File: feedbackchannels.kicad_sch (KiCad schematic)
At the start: 75 parts

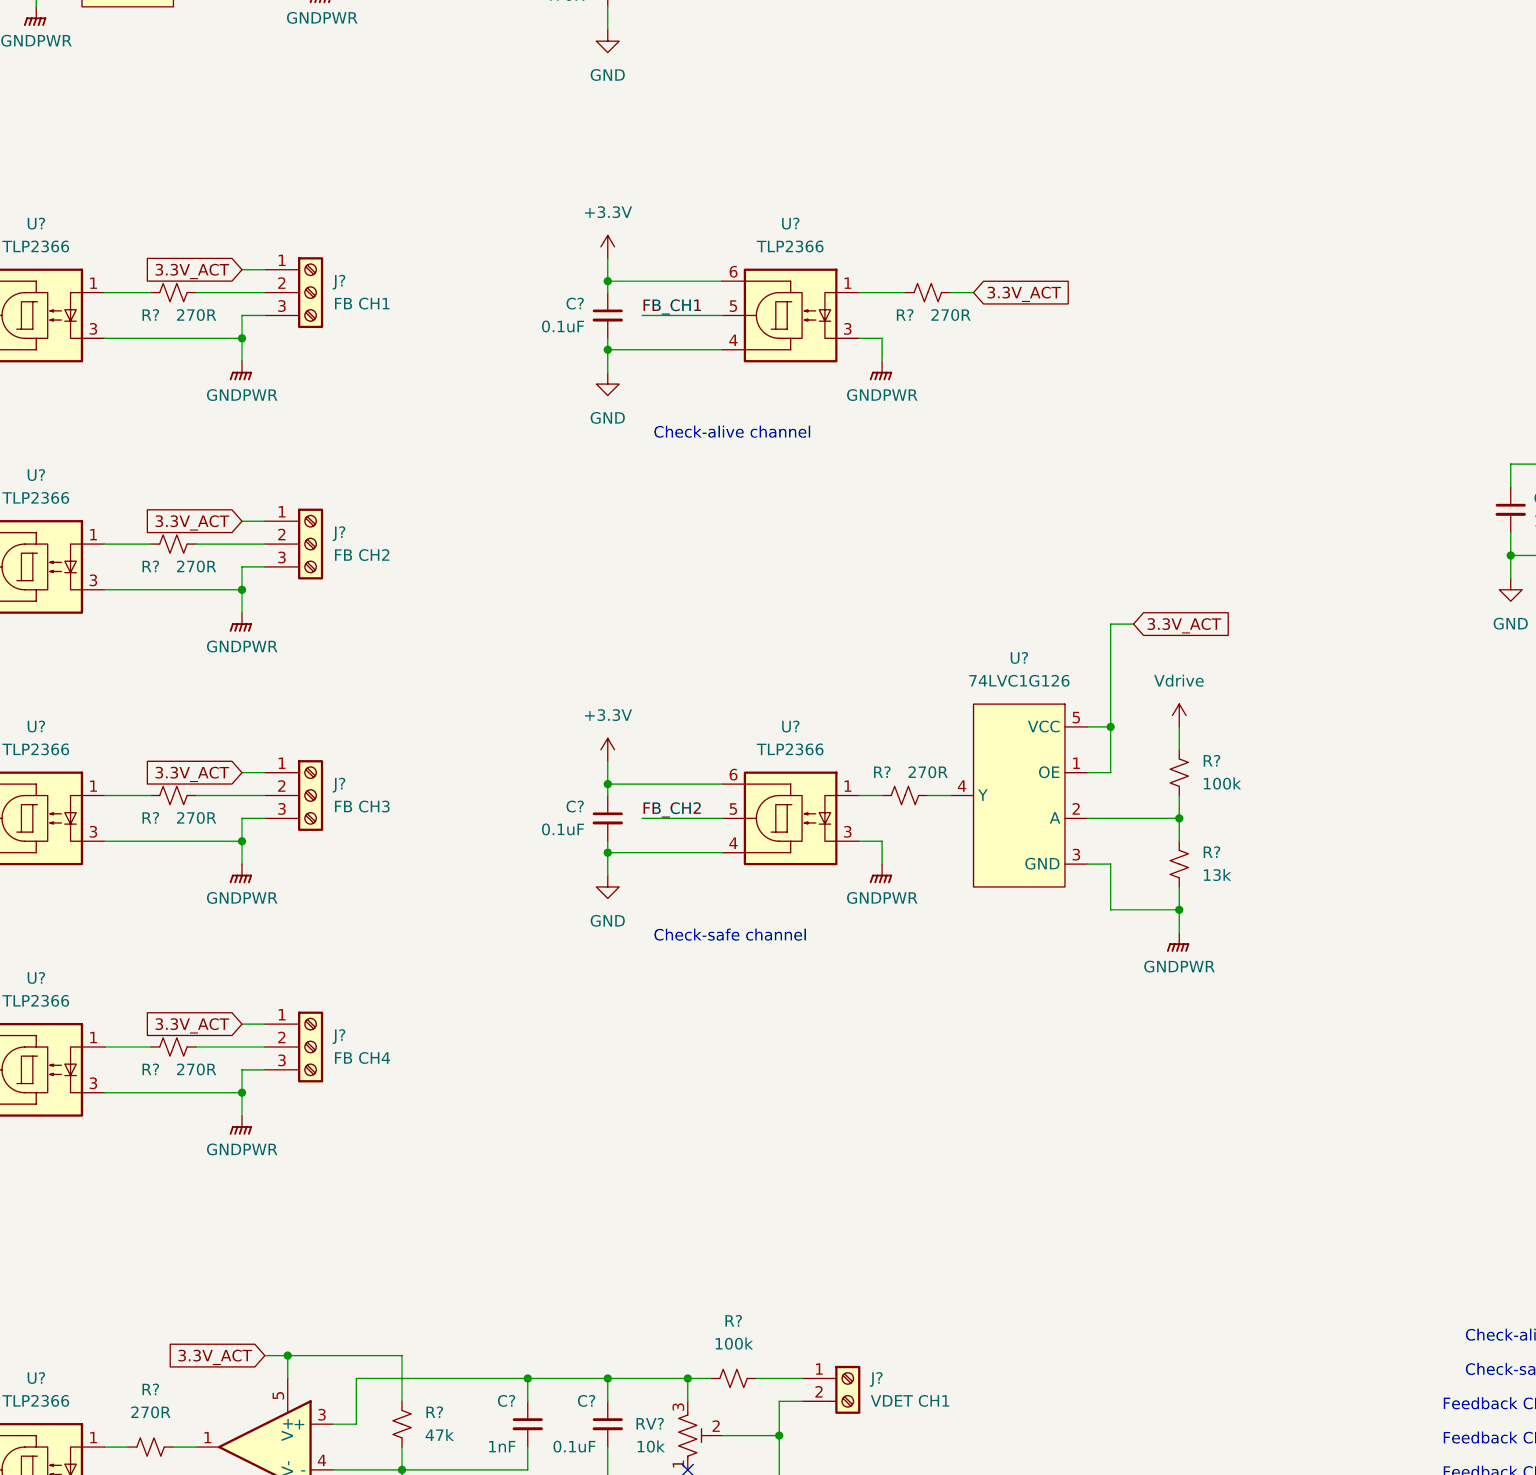
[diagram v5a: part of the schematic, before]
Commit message: add text
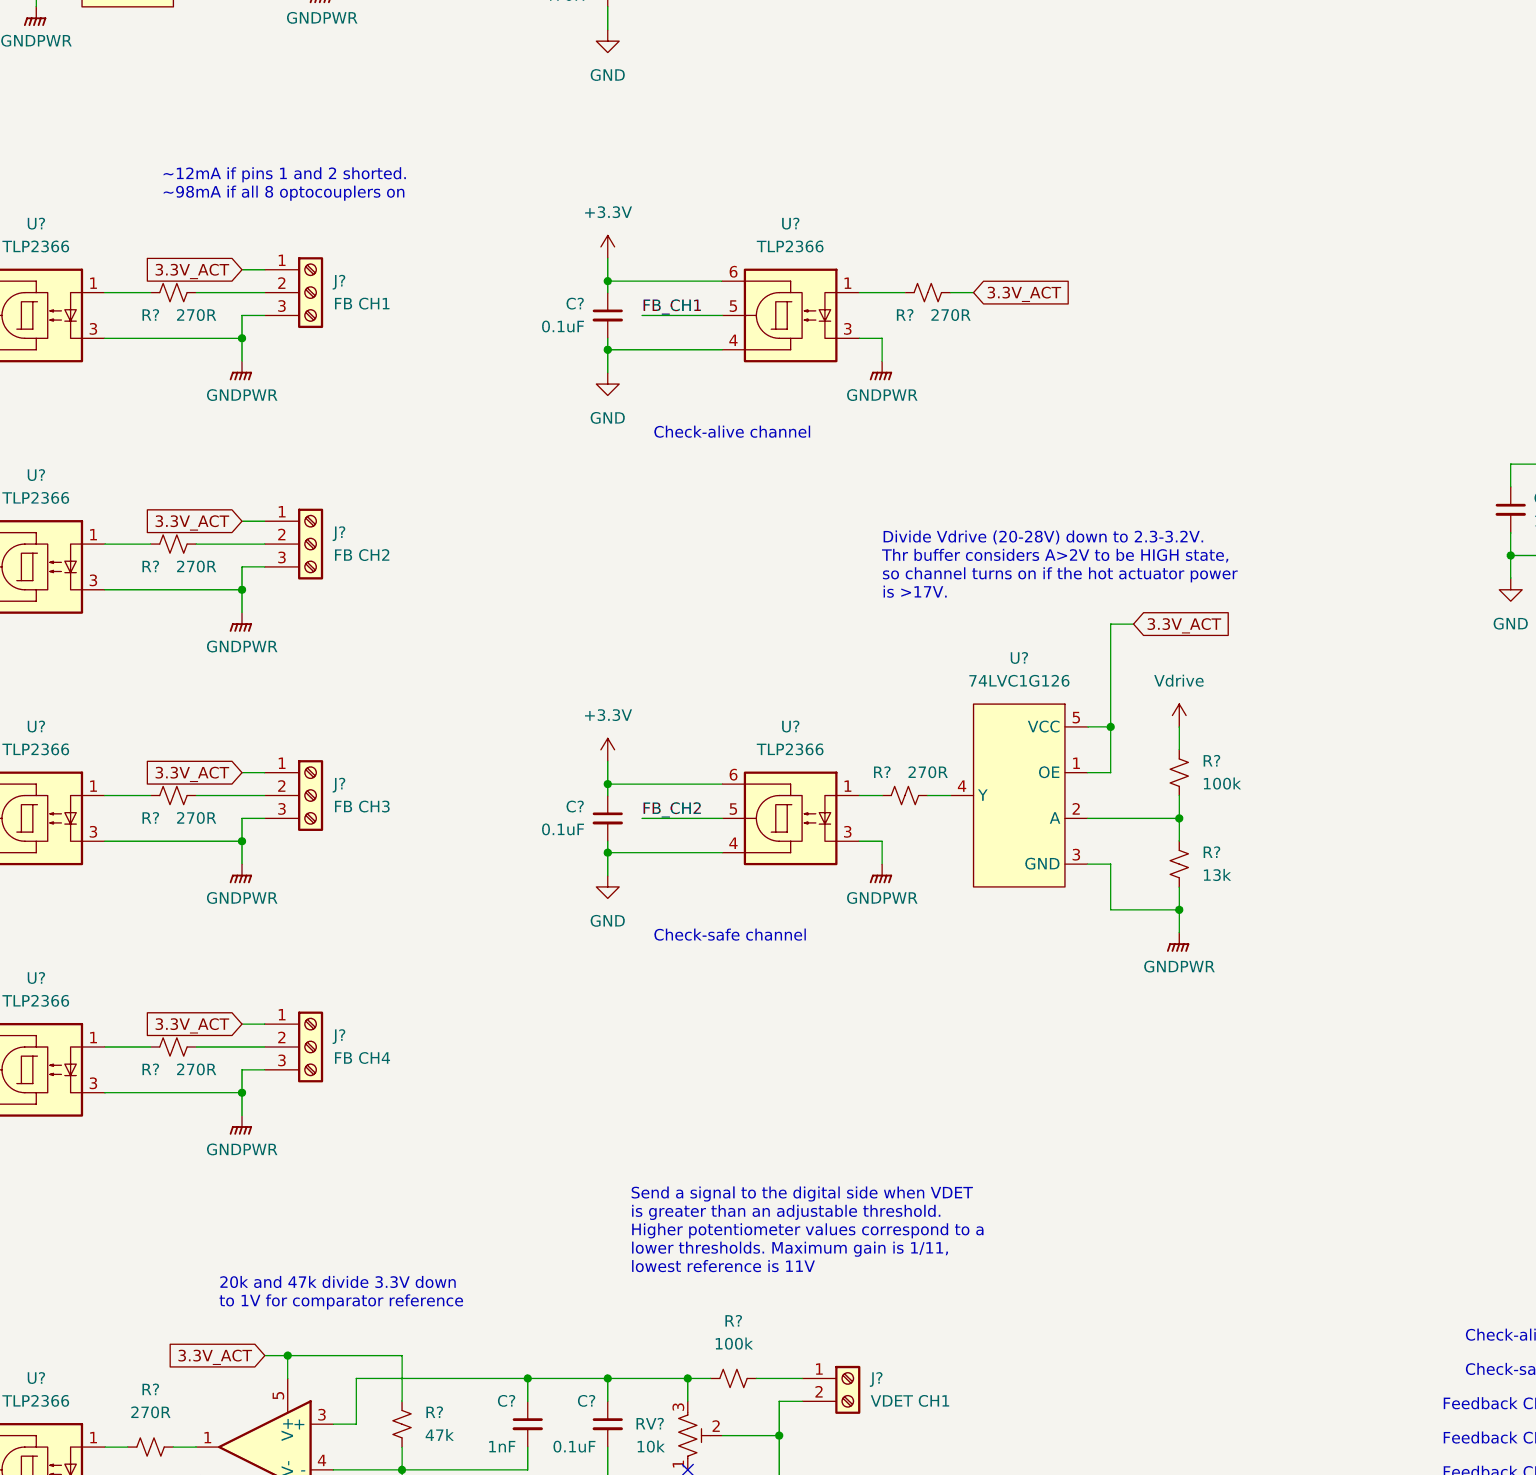
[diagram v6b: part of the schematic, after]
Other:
- note added: "20k and 47k divide 3.3V down to 1V for comparator reference"
- note added: "Divide Vdrive (20-28V) down to 2.3-3.2V. Thr buffer considers A>2V to be HIGH state, so channel turns on if the hot actuator power is >17V."
- note added: "Send a signal to the digital side when VDET is greater than an adjustable threshold. Higher potentiometer values correspond to a lower thresholds. Maximum gain is 1/11, lowest reference is 11V"
- note added: "~12mA if pins 1 and 2 shorted. ~98mA if all 8 optocouplers on"

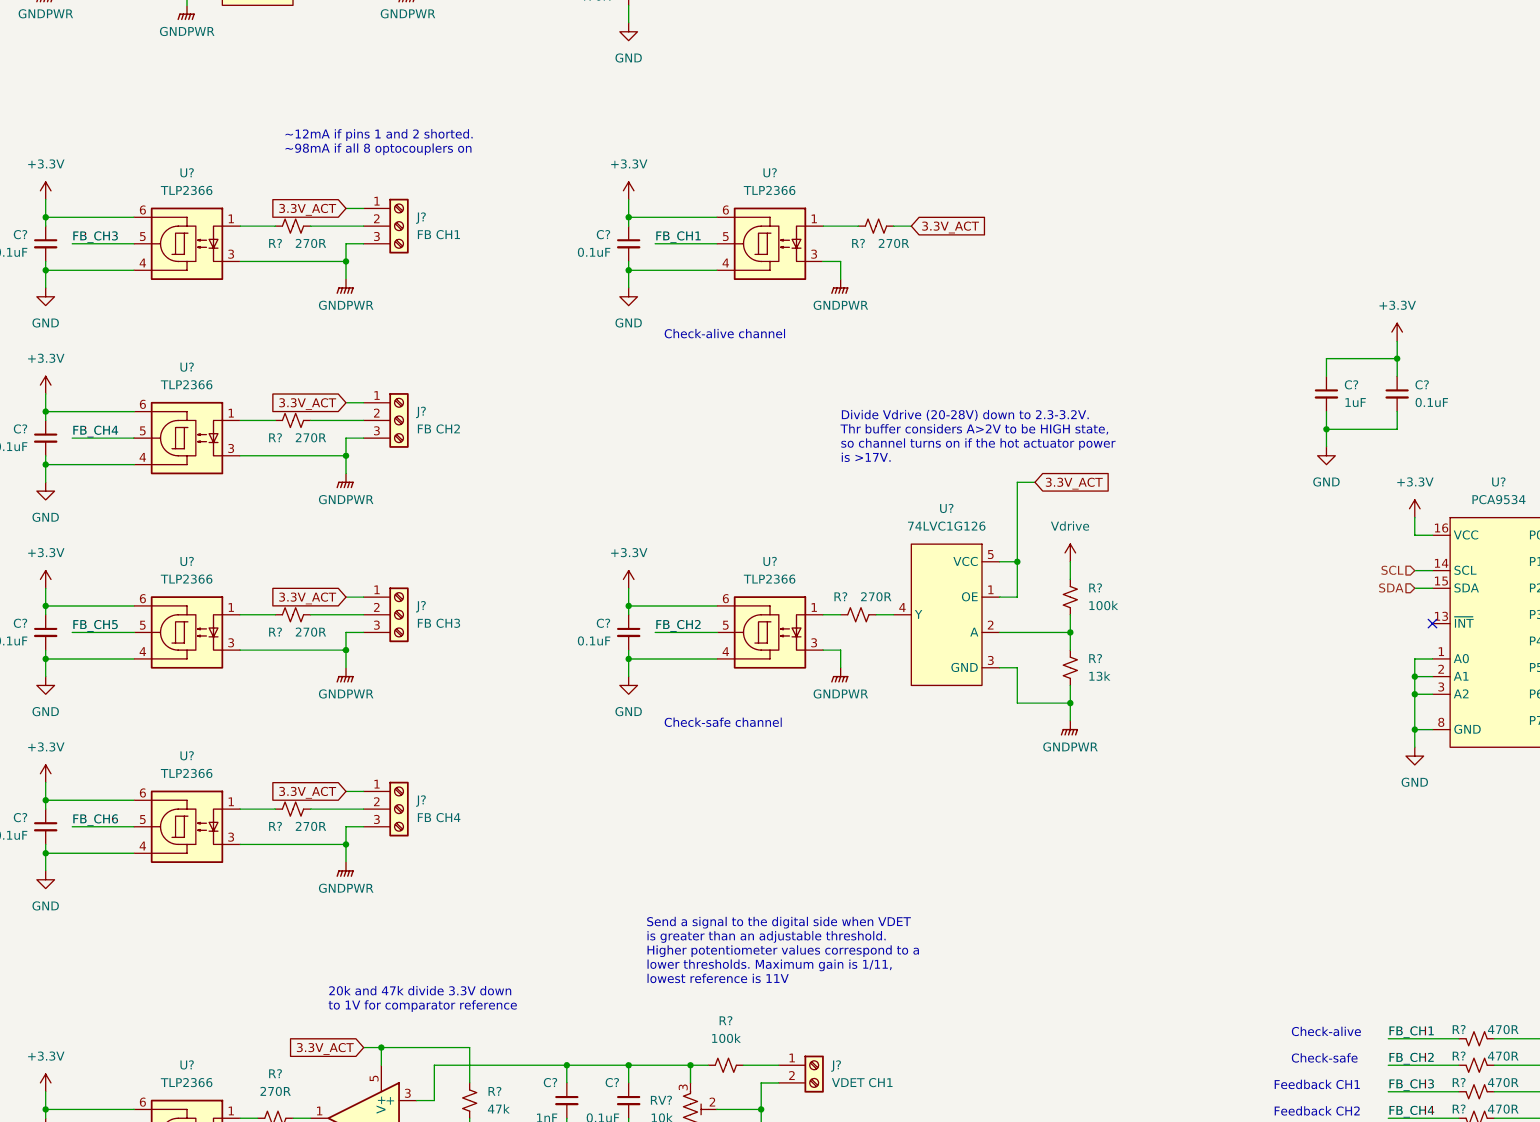
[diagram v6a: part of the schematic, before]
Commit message: Created arming circuit controllable by C&C
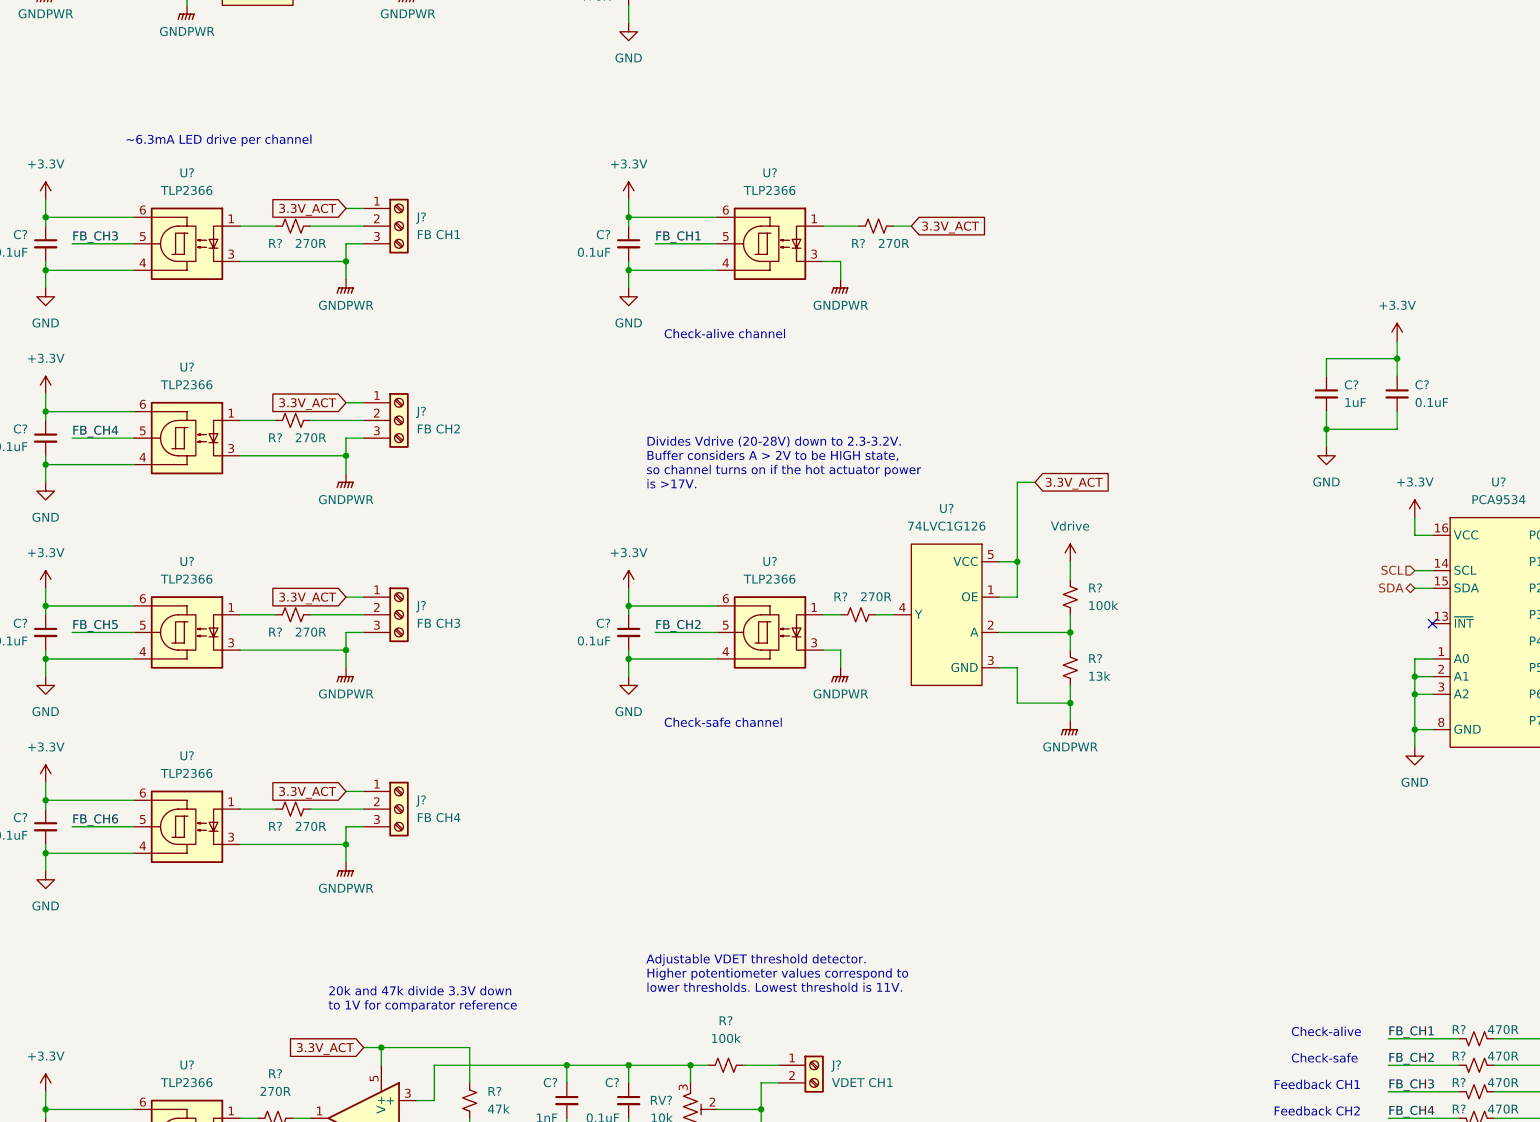
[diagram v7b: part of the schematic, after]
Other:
- note added: "Adjustable VDET threshold detector. Higher potentiometer values correspond to lower thresholds. Lowest threshold is 11V."
- note added: "Divides Vdrive (20-28V) down to 2.3-3.2V. Buffer considers A > 2V to be HIGH state, so channel turns on if the hot actuator power is >17V."
- note added: "~6.3mA LED drive per channel"
- note removed: "Divide Vdrive (20-28V) down to 2.3-3.2V. Thr buffer considers A>2V to be HIGH state, so channel turns on if the hot actuator power is >17V."
- note removed: "Send a signal to the digital side when VDET is greater than an adjustable threshold. Higher potentiometer values correspond to a lower thresholds. Maximum gain is 1/11, lowest reference is 11V"
- note removed: "~12mA if pins 1 and 2 shorted. ~98mA if all 8 optocouplers on"
